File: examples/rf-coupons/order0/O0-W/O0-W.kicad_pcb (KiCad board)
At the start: 4 copper layers, 57.5 x 131.2 mm, 38 parts, among them X16 Anchor, X18 Anchor, X29 Anchor, X32 Anchor, X35 Anchor

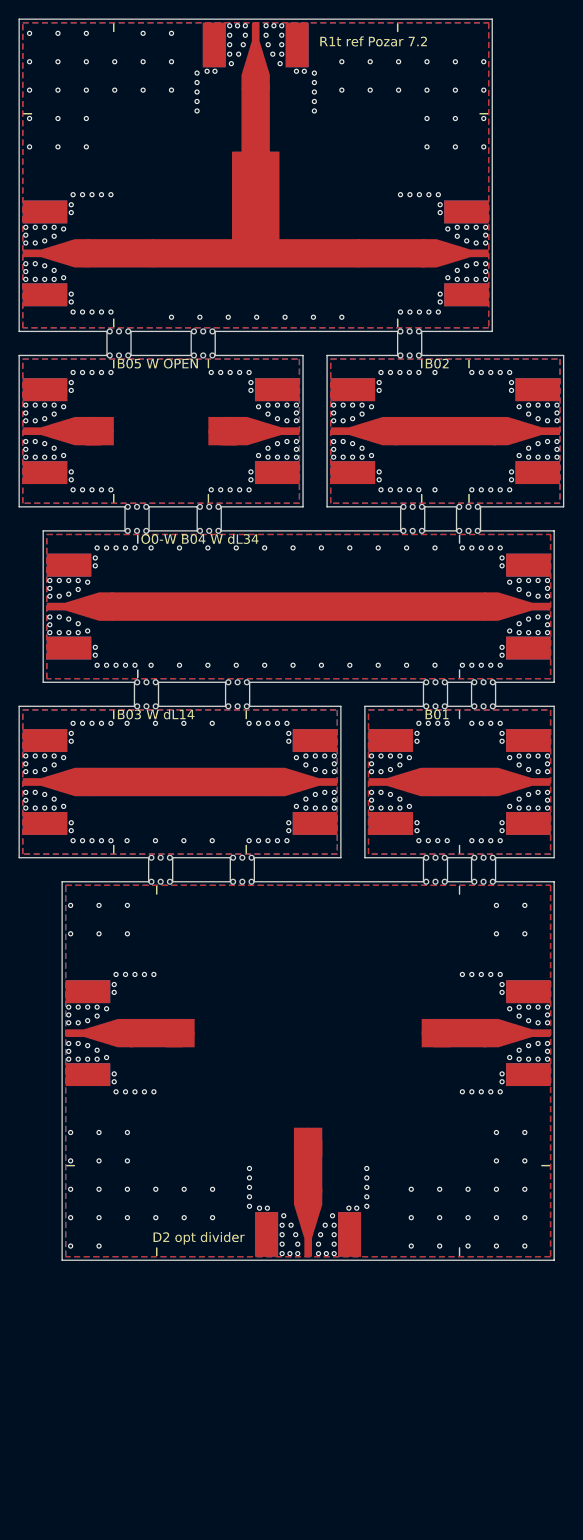
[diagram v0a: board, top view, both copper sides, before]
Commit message: Order 0: regenerate O0-W with D2, QR label stick, GUI-KiCad guard
O0-W now ships d2-star-sched (compute.md's recommendation, the pre-registered
|S11|-missing near-miss) with real copper, not the stale placeholder: the
committed board and catalog.json predate catalog.o_optimized's D2 wiring.
KiCad DRC 0 errors/0 warnings, yapnr fab build 0 errors (headless kicad-cli
10.0.6).

- layout_o.tag_stick: a small-stick mode (no microsection/meander duty) for a
  QR-only label when the full A15 stick doesn't fit the panel.
- catalog._label_stick + wiring: O0-D's "A15" and O0-W's "B15", a 25 x 25 mm
  QR to each board's docs page (reusing o_optimized's docs_url). Neither
  board had a docs link on it before (only O0-M's own A15 did).
- catalog.o_optimized: a winner's footprint path is now stored repo-relative
  in catalog.json ("islands.source"), not the absolute path it was called
  with -- the absolute machine path was tripping the privacy scan on O0-W's
  first real (non-placeholder) catalog.json commit.
- fab.kicad_cli: refuses a GUI KiCad.app (or any non-background-only app
  bundle) rather than silently using it for a real OSH Park order's DRC and
  fab package (DEVELOPERS.md#kicad); self-contained, no new Bazel dep.
- preregistration.md: records the owner's default -- d2-star-sched ships on
  O0-W unless the owner says otherwise -- next to the existing "owner's call"
  row, which stays the binding text.
- tests/unit/rf_coupons/test_order0.py: the new A15/B15 ids and the panel
  size limits the QR stick grows O0-D (7.24 -> 9.16 sq in) and O0-W
  (11.70 -> 13.28 sq in) to.

O0-D stays the placeholder: d1-star's committed footprint still has its two
known 0.100 mm corner-gap violations (OSH Park's 0.127 mm rule), confirmed
with a fresh headless KiCad DRC run (2 clearance errors) -- the D1
re-optimization campaign (20261005-mceval-f1e549) that would fix this is
still running, tracked separately. Regenerating O0-D now would ship a board
that fails its own fab DRC, so it is l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
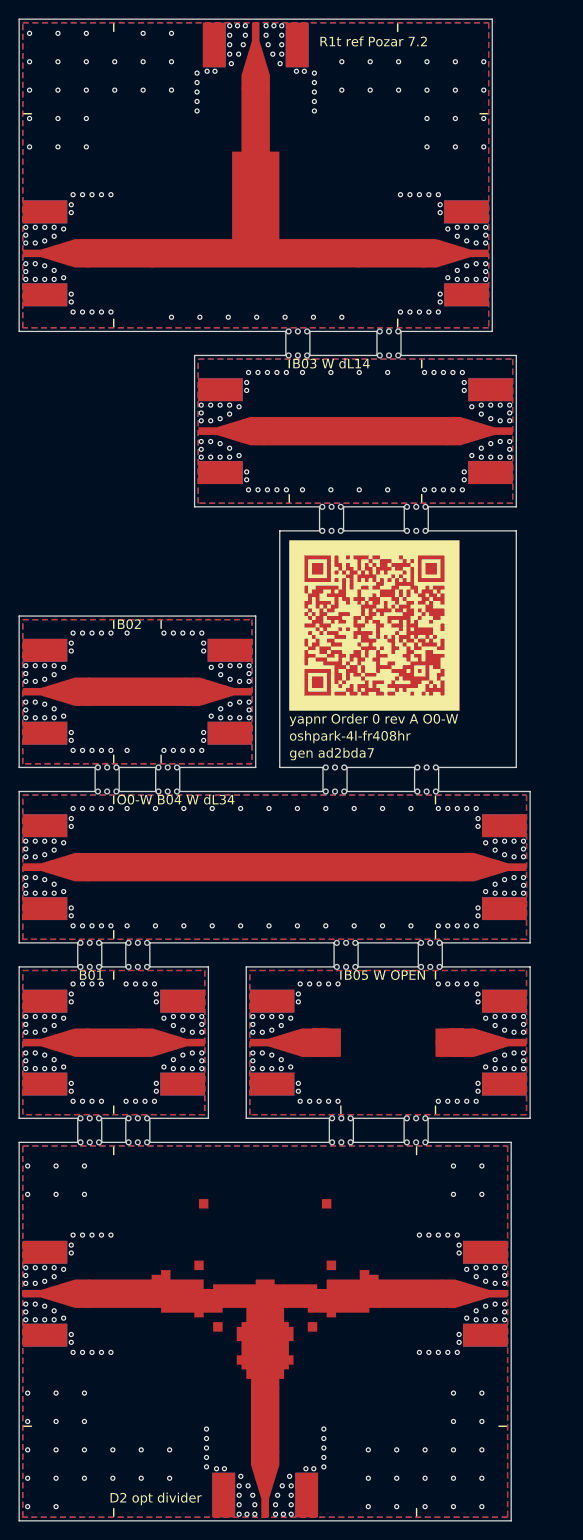
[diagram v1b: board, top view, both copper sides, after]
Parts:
- removed PHD2: Placeholder_D2, Placeholder_D2
- removed X29, X32, X35: Anchor, Anchor
- added UD2: Optimized_D2, Optimized_D2, F.Cu at (46.0, 154.7)
- moved MO_B05L 68.9 mm to (46.5, 122.5)
- moved JB05E 68.9 mm to (74.0, 128.2)
- moved JB05W 68.9 mm to (44.0, 128.2)
- moved X16 68.9 mm to (52.5, 128.2)
- moved X18 68.9 mm to (65.5, 128.2)
- moved MO_B05R 68.9 mm to (59.8, 122.5)
- moved MO_B01 45.8 mm to (22.5, 122.5)
- moved JB01E 45.8 mm to (40.0, 128.2)
- moved JB01W 45.8 mm to (20.0, 128.2)
- moved MO_B02 42.6 mm to (22.5, 85.4)
- moved JB02E 42.6 mm to (45.0, 91.1)
- moved JB02W 42.6 mm to (20.0, 91.1)
- moved MO_B03 41.5 mm to (41.0, 57.8)
- moved JB03E 41.5 mm to (72.5, 63.5)
- moved JB03W 41.5 mm to (38.5, 63.5)
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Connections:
- JD2_1 pad 1: RF_D2_1 -> RF_D2
- JD2_2 pad 1: RF_D2_2 -> RF_D2
- JD2_3 pad 1: RF_D2_3 -> RF_D2
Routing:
- net RF_D2: track 0.00 -> 19.8 mm
- net RF_D2_3: track 5.09 -> 0.00 mm
- net RF_D2_2: track 5.09 -> 0.00 mm
- net RF_D2_1: track 5.09 -> 0.00 mm
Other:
- board size 57.5 x 131.2 mm -> 54 x 158.7 mm
- board text added: "03b7d938"
- board text added: "O0-W B15"
- board text added: "gen ad2bda7"
- board text added: "oshpark-4l-fr408hr"
- board text added: "yapnr Order 0 rev A O0-W"
- board text removed: "D2 window 20 x 24"
